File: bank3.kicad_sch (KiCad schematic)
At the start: 18 parts, among them U12 41256, U13 41256, U14 41256, U20 41256, U21 41256, U22 41256, U28 41256, U29 41256, U30 41256, U36 41256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

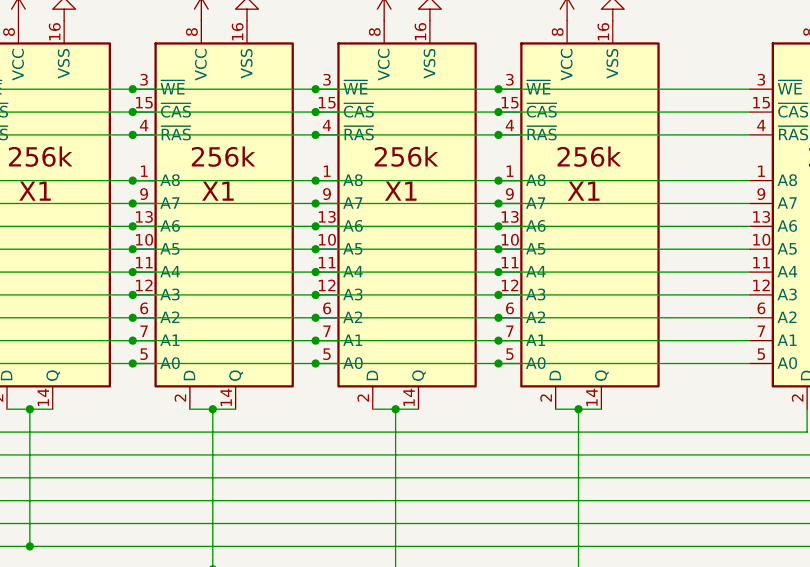
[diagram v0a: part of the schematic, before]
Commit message: updates to match compaq design
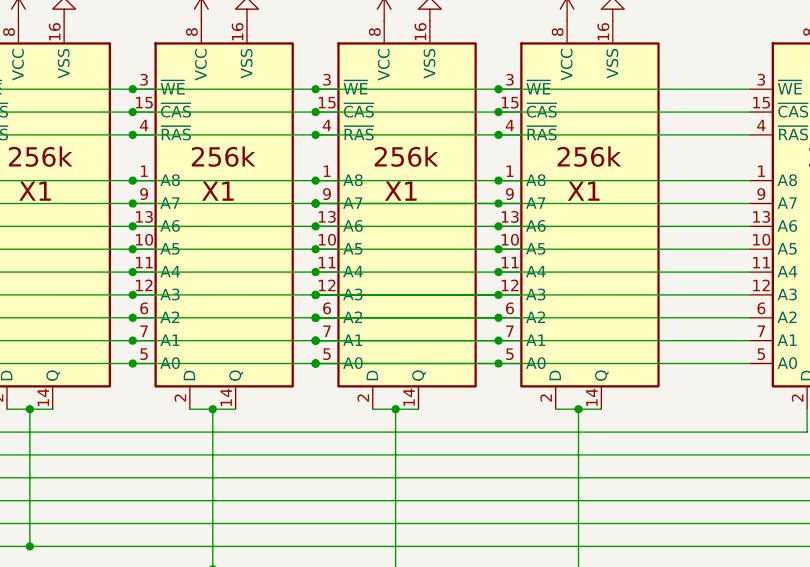
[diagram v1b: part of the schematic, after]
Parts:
- U12, U13, U14, U20, U21, U22, U28, U29, U30, U36, U37, U38, U4, U44, U45, U46, U5, U6: footprint Package_DIP:DIP-16_W7.62mm -> Library:DIP-16_W7.62mm_Socket
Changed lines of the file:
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@@
 	)
 	(junction
+		(at 157.48 55.88)
+		(diameter 0)
+		(color 0 0 0 0)
+	)
+	(junction
 		(at 177.8 134.62)
 		(diameter 0)
@@
 	)
 	(junction
+		(at 157.48 45.72)
+		(diameter 0)
+		(color 0 0 0 0)
+	)
+	(junction
 		(at 35.56 116.84)
 		(diameter 0)
@@
 	)
 	(junction
+		(at 157.48 60.96)
+		(diameter 0)
+		(color 0 0 0 0)
+	)
+	(junction
 		(at 116.84 139.7)
 		(diameter 0)
@@
 	)
 	(junction
+		(at 157.48 63.5)
+		(diameter 0)
+		(color 0 0 0 0)
+	)
+	(junction
 		(at 96.52 114.3)
 		(diameter 0)
@@
 	)
 	(junction
+		(at 157.48 58.42)
+		(diameter 0)
+		(color 0 0 0 0)
+	)
+	(junction
 		(at 116.84 127)
 		(diameter 0)
@@
 	(wire
 		(pts
+			(xy 157.48 55.88) (xy 177.8 55.88)
+		)
+		(stroke
+			(width 0)
+			(type default)
+		)
+	)
+	(wire
+		(pts
 			(xy 146.05 68.58) (xy 148.59 68.58)
 		)
@@
 	(wire
 		(pts
+			(xy 157.48 58.42) (xy 177.8 58.42)
+		)
+		(stroke
+			(width 0)
+			(type default)
+		)
+	)
+	(wire
+		(pts
 			(xy 25.4 127) (xy 35.56 127)
 		)
@@
 	(wire
 		(pts
+			(xy 157.48 63.5) (xy 177.8 63.5)
+		)
+		(stroke
+			(width 0)
+			(type default)
+		)
+	)
+	(wire
+		(pts
+			(xy 157.48 45.72) (xy 177.8 45.72)
+		)
+		(stroke
+			(width 0)
+			(type default)
+		)
+	)
+	(wire
+		(pts
 			(xy 35.56 35.56) (xy 55.88 35.56)
 		)
@@
 	(wire
 		(pts
+			(xy 157.48 60.96) (xy 177.8 60.96)
+		)
+		(stroke
+			(width 0)
+			(type default)
+		)
+	)
+	(wire
+		(pts
 			(xy 85.09 147.32) (xy 87.63 147.32)
 		)
@@
 			)
 		)
-		(property "Footprint" "Package_DIP:DIP-16_W7.62mm"
+		(property "Footprint" "Library:DIP-16_W7.62mm_Socket"
 			(at 208.28 125.73 0)
 			(effects
@@
 			)
 		)
-		(property "Footprint" "Package_DIP:DIP-16_W7.62mm"
+		(property "Footprint" "Library:DIP-16_W7.62mm_Socket"
 			(at 147.32 46.99 0)
 			(effects
@@
 			)
 		)
-		(property "Footprint" "Package_DIP:DIP-16_W7.62mm"
+		(property "Footprint" "Library:DIP-16_W7.62mm_Socket"
 			(at 167.64 46.99 0)
 			(effects
@@
 			)
 		)
-		(property "Footprint" "Package_DIP:DIP-16_W7.62mm"
+		(property "Footprint" "Library:DIP-16_W7.62mm_Socket"
 			(at 236.22 125.73 0)
 			(effects
@@
 			)
 		)
-		(property "Footprint" "Package_DIP:DIP-16_W7.62mm"
+		(property "Footprint" "Library:DIP-16_W7.62mm_Socket"
 			(at 187.96 46.99 0)
 			(effects
@@
 			)
 		)
-		(property "Footprint" "Package_DIP:DIP-16_W7.62mm"
+		(property "Footprint" "Library:DIP-16_W7.62mm_Socket"
 			(at 167.64 125.73 0)
 			(effects
@@
 			)
 		)
-		(property "Footprint" "Package_DIP:DIP-16_W7.62mm"
+		(property "Footprint" "Library:DIP-16_W7.62mm_Socket"
 			(at 187.96 125.73 0)
 			(effects
@@
 			)
 		)
-		(property "Footprint" "Package_DIP:DIP-16_W7.62mm"
+		(property "Footprint" "Library:DIP-16_W7.62mm_Socket"
 			(at 106.68 46.99 0)
 			(effects
@@
 			)
 		)
-		(property "Footprint" "Package_DIP:DIP-16_W7.62mm"
+		(property "Footprint" "Library:DIP-16_W7.62mm_Socket"
 			(at 66.04 125.73 0)
 			(effects
@@
 			)
 		)
-		(property "Footprint" "Package_DIP:DIP-16_W7.62mm"
+		(property "Footprint" "Library:DIP-16_W7.62mm_Socket"
 			(at 86.36 125.73 0)
 			(effects
@@
 			)
 		)
-		(property "Footprint" "Package_DIP:DIP-16_W7.62mm"
+		(property "Footprint" "Library:DIP-16_W7.62mm_Socket"
 			(at 127 125.73 0)
 			(effects
@@
 			)
 		)
-		(property "Footprint" "Package_DIP:DIP-16_W7.62mm"
+		(property "Footprint" "Library:DIP-16_W7.62mm_Socket"
 			(at 106.68 125.73 0)
 			(effects
@@
 			)
 		)
-		(property "Footprint" "Package_DIP:DIP-16_W7.62mm"
+		(property "Footprint" "Library:DIP-16_W7.62mm_Socket"
 			(at 86.36 46.99 0)
 			(effects
@@
 			)
 		)
-		(property "Footprint" "Package_DIP:DIP-16_W7.62mm"
+		(property "Footprint" "Library:DIP-16_W7.62mm_Socket"
 			(at 236.22 46.99 0)
 			(effects
@@
 			)
 		)
-		(property "Footprint" "Package_DIP:DIP-16_W7.62mm"
+		(property "Footprint" "Library:DIP-16_W7.62mm_Socket"
 			(at 208.28 46.99 0)
 			(effects
@@
 			)
 		)
-		(property "Footprint" "Package_DIP:DIP-16_W7.62mm"
+		(property "Footprint" "Library:DIP-16_W7.62mm_Socket"
 			(at 147.32 125.73 0)
 			(effects
@@
 			)
 		)
-		(property "Footprint" "Package_DIP:DIP-16_W7.62mm"
+		(property "Footprint" "Library:DIP-16_W7.62mm_Socket"
 			(at 127 46.99 0)
 			(effects
@@
 			)
 		)
-		(property "Footprint" "Package_DIP:DIP-16_W7.62mm"
+		(property "Footprint" "Library:DIP-16_W7.62mm_Socket"
 			(at 66.04 46.99 0)
 			(effects
